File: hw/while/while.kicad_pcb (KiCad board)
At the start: 2 copper layers, 38.4 x 58.9 mm, 22 parts, among them J1 conn_trigger, J2 conn_done, J3 FTDI, J4 conn_active, J5 conn_condition, J6 cond_select, SW2 switch_active, SW3 switch_reset, U1 ATmega328P-PU, Y1 Crystal

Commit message: update hardware
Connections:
- H1 pad 1: GND -> Net-(H1-Pad1)
- H2 pad 1: GND -> Net-(H2-Pad1)
- H3 pad 1: GND -> Net-(H3-Pad1)
- H4 pad 1: GND -> Net-(H4-Pad1)
- SW2 pad 4: Net-(SW2-Pad3) -> Net-(SW2-Pad4)
- SW3 pad 4: Net-(SW3-Pad3) -> Net-(SW3-Pad4)
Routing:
- net GND: track 220.9 -> 194.4 mm
- net a4: track 29.7 -> 23.4 mm
- net Net-(SW3-Pad3): track 4.50 -> 0.00 mm
- net Net-(SW2-Pad3): track 4.50 -> 0.00 mm
- net condSelect: track 20.0 -> 18.1 mm
- net a3: track 41.3 -> 42.0 mm
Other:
- board text added: "v1.1"
- board text removed: "v1"

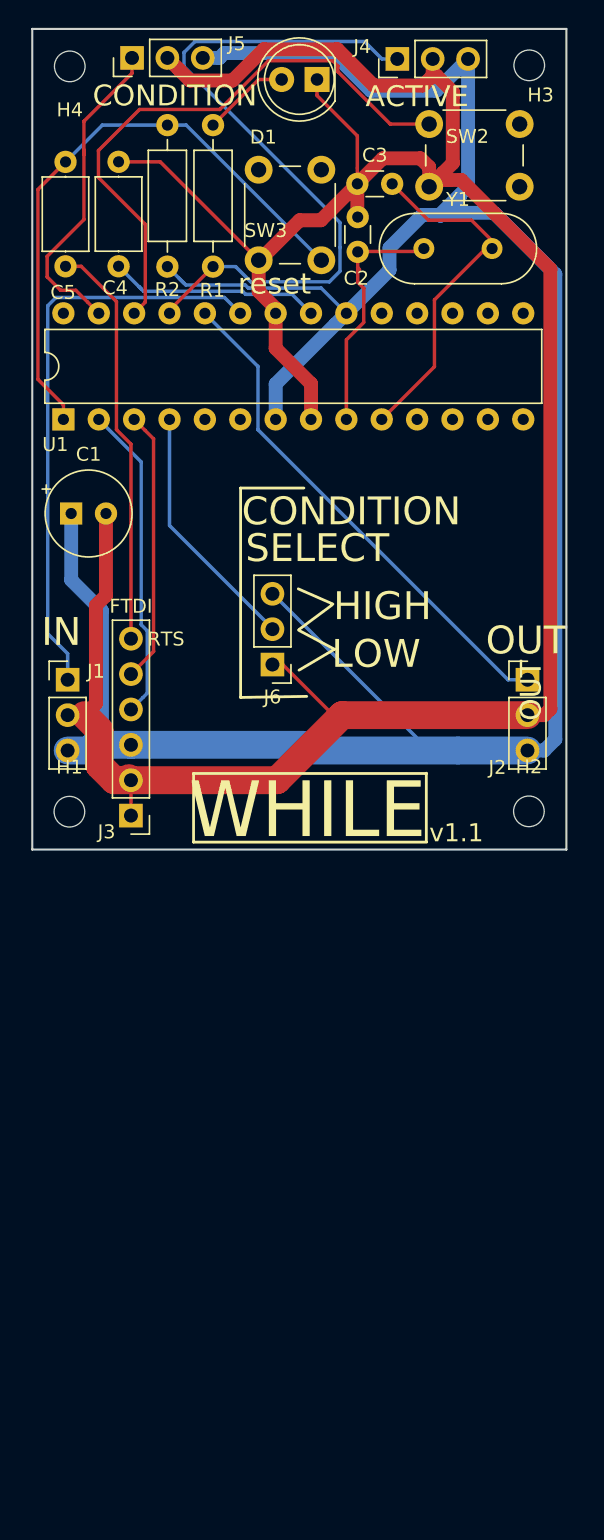
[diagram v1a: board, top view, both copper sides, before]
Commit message: WHILE block v2
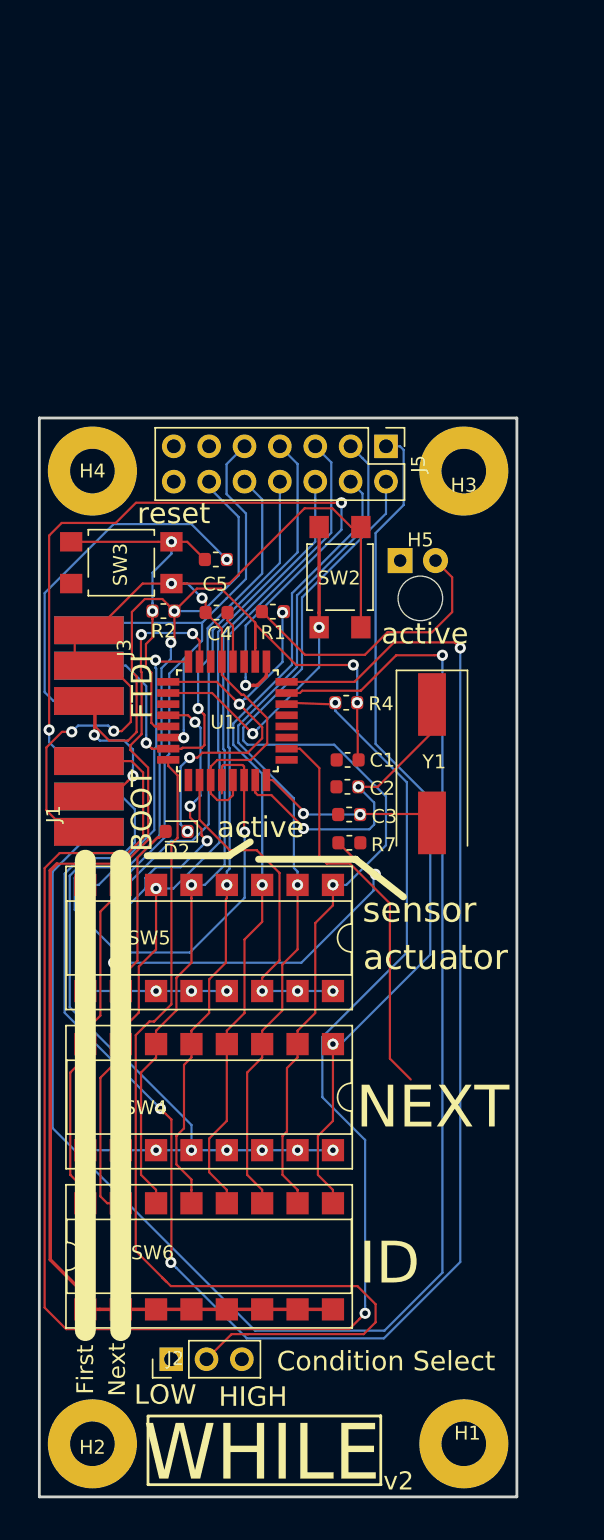
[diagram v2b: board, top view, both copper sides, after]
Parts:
- removed J4: conn_active, Connector_PinHeader_2.54mm:PinHeader_1x03_P2.54mm_Vertical
- removed J6: cond_select, Connector_PinHeader_2.54mm:PinHeader_1x03_P2.54mm_Vertical
- added D2: DIODE, Diode_SMD:D_0603_1608Metric, F.Cu at (134.1, 122.7)
- added H5: led_spy_hole, MountingHole:MountingHole_3.2mm_M3, F.Cu at (151.6, 105.9)
- added R4: 10k, Resistor_SMD:R_0603_1608Metric, F.Cu at (146.2, 113.4)
- added R7: 1k, Resistor_SMD:R_0603_1608Metric, F.Cu at (146.5, 123.5)
- added SW4: NEXT, Package_DIP:DIP-16_W7.62mm_SMDSocket_SmallPads, F.Cu at (136.4, 141.7)
- added SW5: ACTIVE, Package_DIP:DIP-16_W7.62mm_SMDSocket_SmallPads, F.Cu at (136.4, 130.3)
- added SW6: ID, Package_DIP:DIP-16_W7.62mm_SMDSocket_SmallPads, F.Cu at (136.4, 153.2)
- C1: footprint Capacitor_THT:CP_Radial_Tantal_D6.0mm_P2.50mm -> Capacitor_SMD:C_0603_1608Metric
- C2, C3: footprint Capacitor_THT:C_Disc_D3.0mm_W1.6mm_P2.50mm -> Capacitor_SMD:C_0603_1608Metric
- C4, C5: footprint Capacitor_THT:C_Axial_L5.1mm_D3.1mm_P7.50mm_Horizontal -> Capacitor_SMD:C_0603_1608Metric
- D1: moved to B.Cu
- H1, H2, H3, H4: footprint MountingHole:MountingHole_2.2mm_M2 -> MountingHole:MountingHole_3.2mm_M3_Pad
- J1: value conn_trigger -> bootloader; footprint Connector_PinHeader_2.54mm:PinHeader_1x03_P2.54mm_Vertical -> autoblocks:edge_connector_3
- J2: value conn_done -> Conn_01x03_Male
- J3: footprint Connector_PinHeader_2.54mm:PinHeader_1x06_P2.54mm_Vertical -> autoblocks:edge_connector_3
- J5: value conn_condition -> BUS; footprint Connector_PinHeader_2.54mm:PinHeader_1x03_P2.54mm_Vertical -> Connector_PinHeader_2.54mm:PinHeader_2x07_P2.54mm_Vertical
- R1, R2: footprint Resistor_THT:R_Axial_DIN0207_L6.3mm_D2.5mm_P10.16mm_Horizontal -> Resistor_SMD:R_0603_1608Metric
- SW2: value switch_active -> active; footprint autoblocks:SW_PUSH_6mm_H5mm -> Button_Switch_SMD:SW_SPST_TL3305C
- SW3: value switch_reset -> reset; footprint autoblocks:SW_PUSH_6mm_H5mm -> Button_Switch_SMD:SW_SPST_TL3305C
- U1: value ATmega328P-PU -> ATmega328-AU; footprint Package_DIP:DIP-28_W7.62mm -> Package_QFP:TQFP-32_7x7mm_P0.8mm
- Y1: footprint Crystal:Crystal_HC18-U_Vertical -> Crystal:Crystal_SMD_HC49-SD
- moved H2 55.2 mm to (128.0, 166.6)
- moved J2 55.1 mm to (133.7, 160.6), turned to 90 degrees
- moved H1 53.5 mm to (154.7, 166.6)
- moved C3 45.3 mm to (146.5, 121.4)
- moved C2 40.9 mm to (146.3, 119.4), turned to 0 degrees
- moved Y1 37.0 mm to (152.4, 117.8), turned to 270 degrees
- moved R1 35.2 mm to (141.0, 106.9), turned to 0 degrees
- moved D1 35.1 mm to (150.1, 103.2), turned to 0 degrees
- moved J5 33.3 mm to (149.1, 95.0), turned to 270 degrees
- moved SW2 33.2 mm to (145.8, 104.4), turned to 90 degrees
- moved C5 30.5 mm to (136.9, 103.1), turned to 0 degrees
- moved H3 29.5 mm to (154.7, 96.8)
- moved H4 29.1 mm to (128.0, 96.8)
- moved C1 26.6 mm to (146.3, 117.5), turned to 180 degrees
- moved C4 25.8 mm to (136.9, 106.9), turned to 180 degrees
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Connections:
- C1 pad 1: VCC -> bus11
- C1 pad 2: GND -> bus13
- C2 pad 1: GND -> bus13
- C3 pad 1: GND -> bus13
- C4 pad 2: GND -> bus13
- D1 pad 1: GND -> bus13
- J1 pad 1: a0 -> bus13
- J1 pad 2: GND -> bus11
- J1 pad 3: VCC -> d10
- J2 pad 1: a1 -> bus13
- J2 pad 2: GND -> condSelect
- J2 pad 3: VCC -> bus11
- J3 pad 1: GND -> bus13
- J3 pad 2: GND -> bus13
- J3 pad 3: VCC -> bus11
- J5 pad 1: a4 -> bus1
- J5 pad 2: GND -> bus2
- J5 pad 3: VCC -> bus3
- R2 pad 1: VCC -> bus11
- SW2 pad 2: GND -> bus13
- SW3 pad 1: GND -> bus13
- U1 pad 1: RESET -> d3
- U1 pad 10: XTAL2 -> d6
- U1 pad 11: d5 -> d7
- U1 pad 12: d6 -> d8
- U1 pad 13: d7 -> d9
- U1 pad 14: d8 -> d10
- U1 pad 15: d9 -> d11
- U1 pad 16: d10 -> d12
- U1 pad 17: d11 -> d13
- U1 pad 18: d12 -> bus11
- U1 pad 19: d13 -> Net-(U1-Pad19)
- U1 pad 2: RX -> condition
- U1 pad 20: VCC -> AREF
- U1 pad 21: AREF -> bus13
- U1 pad 22: GND -> Net-(U1-Pad22)
- U1 pad 3: TX -> bus13
- U1 pad 4: condSelect -> bus11
- U1 pad 5: d3 -> bus13
- U1 pad 6: d4 -> bus11
- U1 pad 7: VCC -> XTAL1
- U1 pad 8: GND -> XTAL2
- U1 pad 9: XTAL1 -> d5
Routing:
- net GND: track 194.4 -> 0.00 mm
- net VCC: track 188.2 -> 0.00 mm
- net d10: track 0.00 -> 128.6 mm, vias 0 -> 2
- net bus11: track 0.00 -> 126.8 mm, vias 0 -> 7
- net d12: track 0.00 -> 126.1 mm, vias 0 -> 3
- net d11: track 0.00 -> 114.8 mm, vias 0 -> 1
- net bus13: track 0.00 -> 81.2 mm, vias 0 -> 4
- net bus2: track 0.00 -> 68.0 mm, vias 0 -> 1
- net bus7: track 0.00 -> 63.0 mm, vias 0 -> 1
- net bus3: track 0.00 -> 62.5 mm, vias 0 -> 1
- net bus1: track 0.00 -> 62.1 mm, vias 0 -> 1
- net bus5: track 0.00 -> 60.0 mm, vias 0 -> 1
- net bus8: track 0.00 -> 59.4 mm, vias 0 -> 1
- net d13: track 0.00 -> 59.0 mm, vias 0 -> 3
- net bus4: track 0.00 -> 59.0 mm, vias 0 -> 1
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- added copper zone on B.Cu, net bus11
- added copper zone on F.Cu, net bus13
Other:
- board size 38.4 x 58.9 mm -> 34.3 x 77.5 mm
- rule trace_min: 0.2 -> 0.16
- board text added: "BOOT"
- board text added: "Condition Select"
- board text added: "FTDI"
- board text added: "First"
- board text added: "ID"
- board text added: "NEXT"
- board text added: "Next"
- board text added: "active"
- board text added: "actuator"
- board text added: "sensor"
- board text added: "v2"
- board text removed: "ACTIVE"
- board text removed: "CONDITION"
- board text removed: "IN"
- board text removed: "OUT"
- board text removed: "RTS"
- board text removed: "SELECT"
- board text removed: "v1.1"

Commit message: fix WHILE bus assignemnts
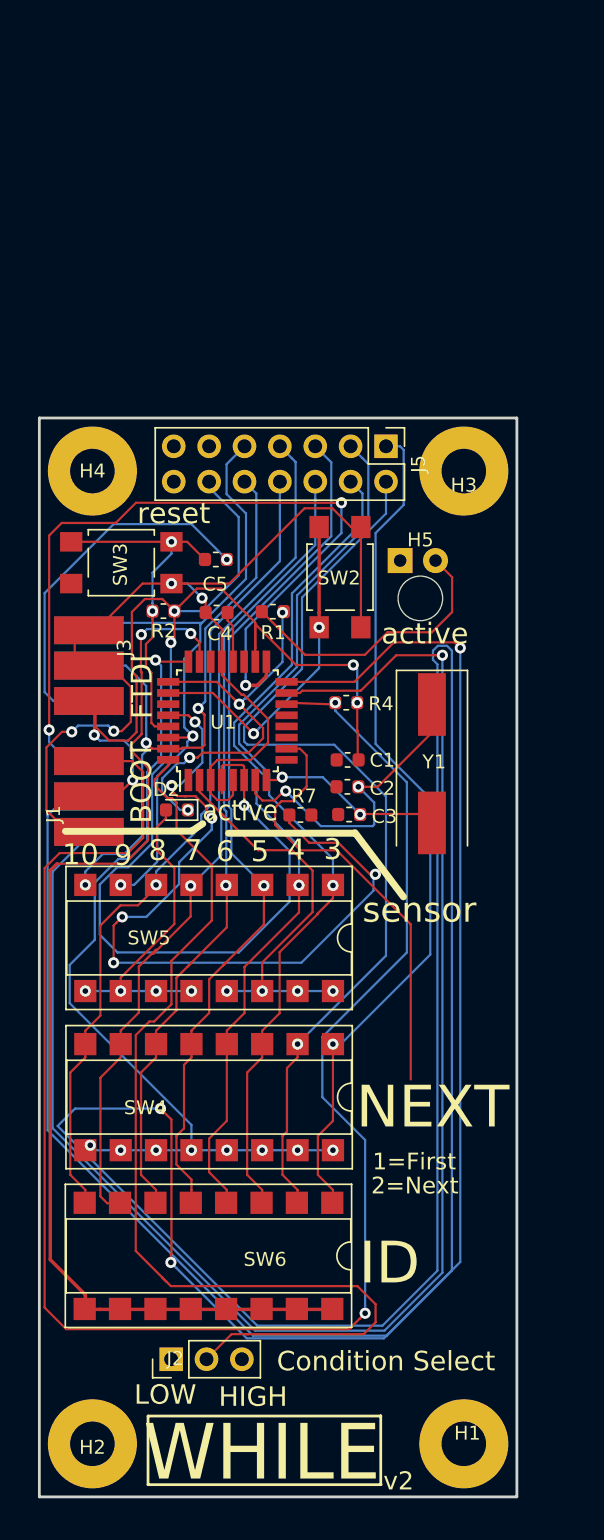
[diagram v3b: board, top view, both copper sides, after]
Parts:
- moved R7 4.05 mm to (142.9, 121.5)
- moved D2 1.54 mm to (134.1, 121.1)
- moved SW6 0.06 mm to (136.3, 153.1), turned to 270 degrees
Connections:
- SW5 pad 1: bus2 -> bus3
- SW5 pad 13: Net-(D2-Pad2) -> condition
- SW5 pad 2: bus3 -> bus4
- SW5 pad 3: bus4 -> bus5
- SW5 pad 4: bus5 -> bus6
- SW5 pad 5: bus6 -> bus7
- SW5 pad 6: bus7 -> bus8
- SW5 pad 7: bus8 -> RX
- SW5 pad 8: RX -> TX
- SW6 pad 1: a0 -> bus1
- SW6 pad 10: bus2 -> a0
- SW6 pad 11: bus3 -> a0
- SW6 pad 12: bus4 -> a0
- SW6 pad 13: bus5 -> a0
- SW6 pad 14: bus6 -> a0
- SW6 pad 15: bus7 -> a0
- SW6 pad 16: bus8 -> a0
- SW6 pad 2: a0 -> bus2
- SW6 pad 3: a0 -> bus3
- SW6 pad 4: a0 -> bus4
- SW6 pad 5: a0 -> bus5
- SW6 pad 6: a0 -> bus6
- SW6 pad 7: a0 -> bus7
- SW6 pad 8: a0 -> bus8
- SW6 pad 9: bus1 -> a0
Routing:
- net d12: track 126.1 -> 291.6 mm
- net TX: track 35.8 -> 48.4 mm, vias 2 -> 3
- net a5: track 49.8 -> 57.3 mm
- net RX: track 55.3 -> 49.4 mm
- net condition: track 24.3 -> 29.1 mm, vias 3 -> 4
- net condSelect: track 70.9 -> 74.0 mm
- net d6: track 29.0 -> 31.8 mm
- net bus4: track 59.0 -> 61.7 mm
- net bus5: track 60.0 -> 62.2 mm
- net bus3: track 62.5 -> 64.6 mm
- net bus11: track 126.8 -> 128.9 mm
- net a1: track 63.3 -> 62.1 mm
- net Net-(D2-Pad2): track 23.9 -> 23.0 mm, vias 5 -> 4
- net bus2: track 68.0 -> 67.4 mm
- net bus7: track 63.0 -> 62.4 mm
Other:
- board text added: "10"
- board text added: "1=First"
- board text added: "2=Next"
- board text added: "3"
- board text added: "4"
- board text added: "5"
- board text added: "6"
- board text added: "7"
- board text added: "8"
- board text added: "9"
- board text removed: "First"
- board text removed: "Next"
- board text removed: "actuator"
